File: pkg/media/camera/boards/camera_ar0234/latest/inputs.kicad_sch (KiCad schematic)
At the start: 10 parts, among them J1 FH34SRJ-22S-0.5SH_50_, Q1 BSS138, Q2 BSS138

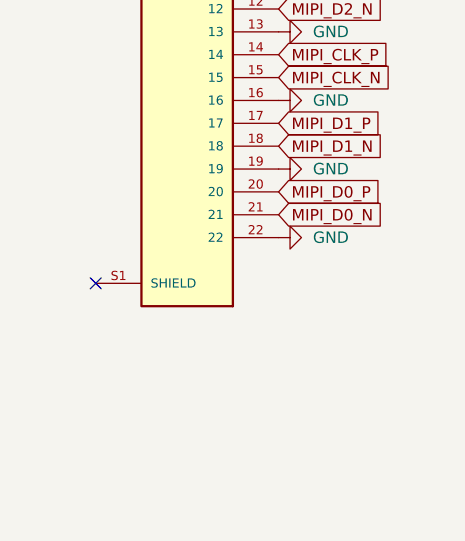
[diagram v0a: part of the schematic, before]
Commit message: Adding more cnc logging logic.
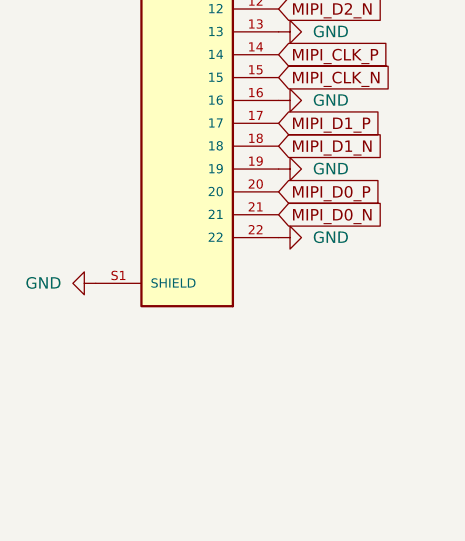
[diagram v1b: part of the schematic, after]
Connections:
- net GND: now also J1.S1 (SHIELD), J1.S2 (SHIELD)
- no-connect marks 1 -> 0
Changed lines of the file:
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@@
 		(color 0 0 0 0)
-	)
-	(no_connect
-		(at 41.91 121.92)
 	)
 	(wire
@@
 					(unit 1)
 				)
+			)
+		)
+	)
+	(symbol
+		(lib_id "power:GND")
+		(at 41.91 121.92 270)
+		(mirror x)
+		(unit 1)
+		(exclude_from_sim no)
+		(in_bom yes)
+		(on_board yes)
+		(dnp no)
+		(fields_autoplaced yes)
+		(property "Reference" "#PWR046"
+			(at 35.56 121.92 0)
+			(effects
+				(font
+					(size 1.27 1.27)
+				)
+				(hide yes)
+			)
+		)
+		(property "Value" "GND"
+			(at 38.1 121.9199 90)
+			(effects
+				(font
+					(size 1.27 1.27)
+				)
+				(justify right)
+			)
+		)
+		(property "Footprint" ""
+			(at 41.91 121.92 0)
+			(effects
+				(font
+					(size 1.27 1.27)
+				)
+				(hide yes)
+			)
+		)
+		(property "Datasheet" ""
+			(at 41.91 121.92 0)
+			(effects
+				(font
+					(size 1.27 1.27)
+				)
+				(hide yes)
+			)
+		)
+		(property "Description" "Power symbol creates a global label with name \"GND\" , ground"
+			(at 41.91 121.92 0)
+			(effects
+				(font
+					(size 1.27 1.27)
+				)
+				(hide yes)
+			)
+		)
+		(pin "1"
+		)
+		(instances
+			(project "board-latest"
+				(path "/2b085460-4688-4840-afb7-ab33185a4ae8/cba96a29-f888-4b60-95bc-d0f548c6d657"
+					(reference "#PWR046")
+					(unit 1)
+				)
